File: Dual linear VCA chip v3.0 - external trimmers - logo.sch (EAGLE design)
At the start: 21 parts, among them IC1 LM13700M, IC2 TL072D, IC3 TL072D, Q1 MMBT3906LT1SMD, Q2 MMBT3906LT1SMD

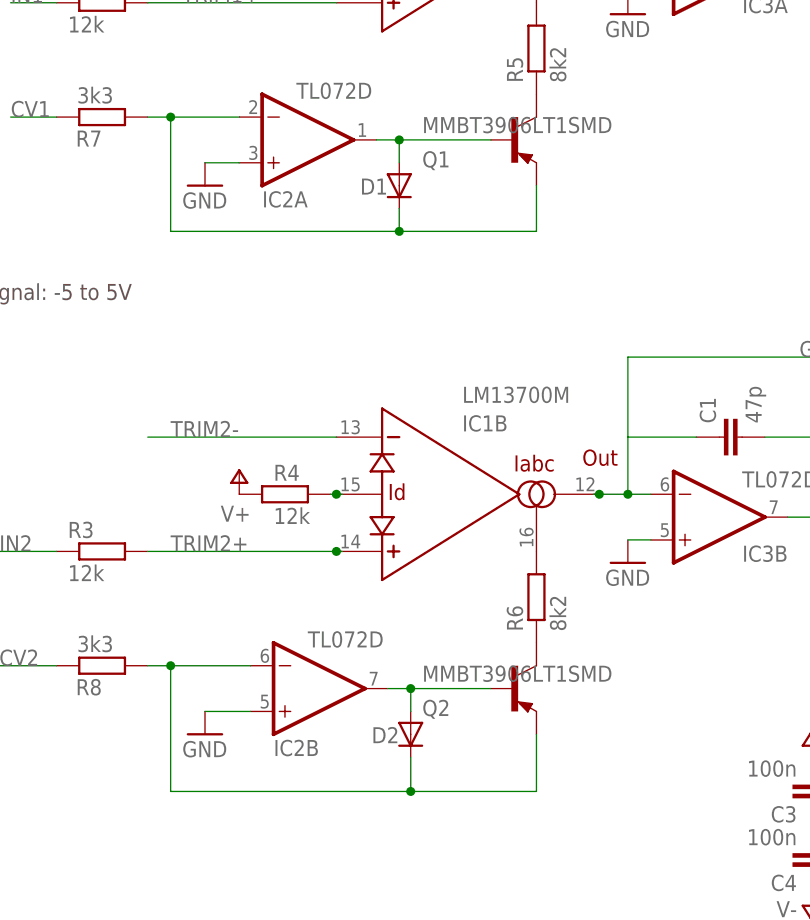
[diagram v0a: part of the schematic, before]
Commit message: Routed v2164-based quad VCA
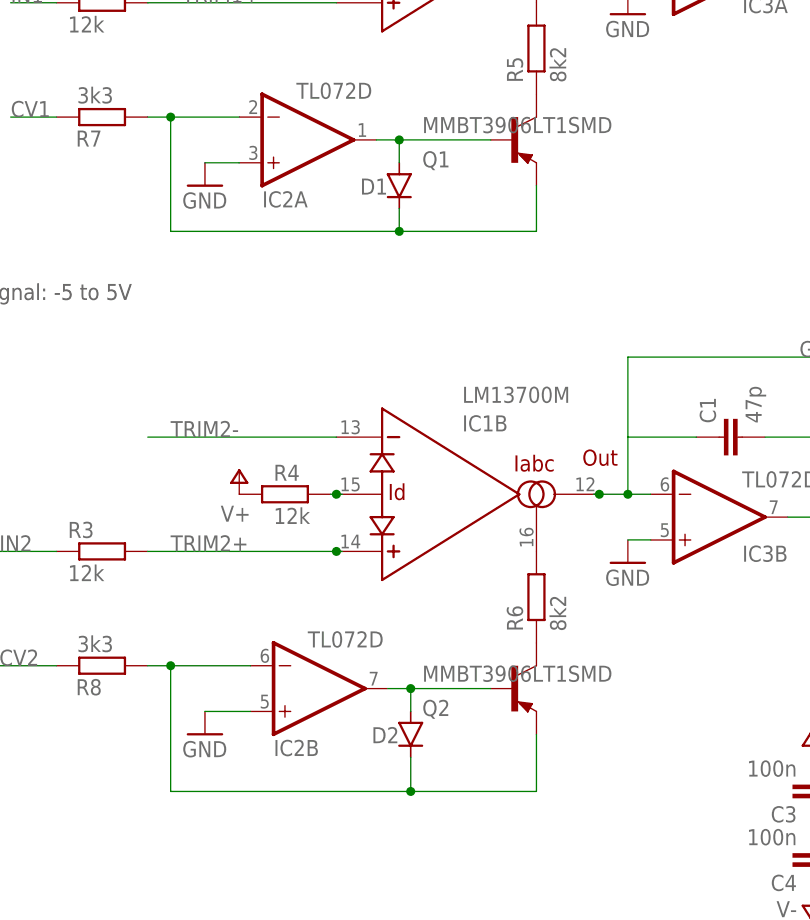
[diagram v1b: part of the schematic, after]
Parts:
- D1, D2: value (none) -> 1N41480805; device diode:DIODE-SOD80C -> joakim:1N41480805
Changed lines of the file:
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@@
 <part name="IC3" library="linear" deviceset="TL072" device="D"/>
 <part name="GND1" library="supply1" deviceset="GND" device=""/>
-<part name="D1" library="diode" deviceset="DIODE-" device="SOD80C"/>
+<part name="D1" library="joakim" deviceset="1N4148" device="0805"/>
 <part name="GND2" library="supply1" deviceset="GND" device=""/>
 <part name="P+1" library="supply1" deviceset="V+" device=""/>
-<part name="D2" library="diode" deviceset="DIODE-" device="SOD80C"/>
+<part name="D2" library="joakim" deviceset="1N4148" device="0805"/>
 <part name="GND5" library="supply1" deviceset="GND" device=""/>
 <part name="GND6" library="supply1" deviceset="GND" device=""/>
@@
 <instance part="D1" gate="G$1" x="53.34" y="44.45" smashed="yes" rot="R270">
 <attribute name="NAME" x="52.07" y="45.2374" size="1.778" layer="95" rot="R180"/>
-<attribute name="VALUE" x="51.0286" y="41.91" size="1.778" layer="96" rot="R270"/>
 </instance>
 <instance part="GND2" gate="1" x="78.74" y="63.5"/>
@@
 <instance part="D2" gate="G$1" x="54.61" y="-16.51" smashed="yes" rot="R270">
 <attribute name="NAME" x="53.34" y="-15.7226" size="1.778" layer="95" rot="R180"/>
-<attribute name="VALUE" x="52.2986" y="-19.05" size="1.778" layer="96" rot="R270"/>
 </instance>
 <instance part="GND5" gate="1" x="31.75" y="-16.51"/>
